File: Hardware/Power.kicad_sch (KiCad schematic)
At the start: 3 parts, among them J18 Conn_01x02

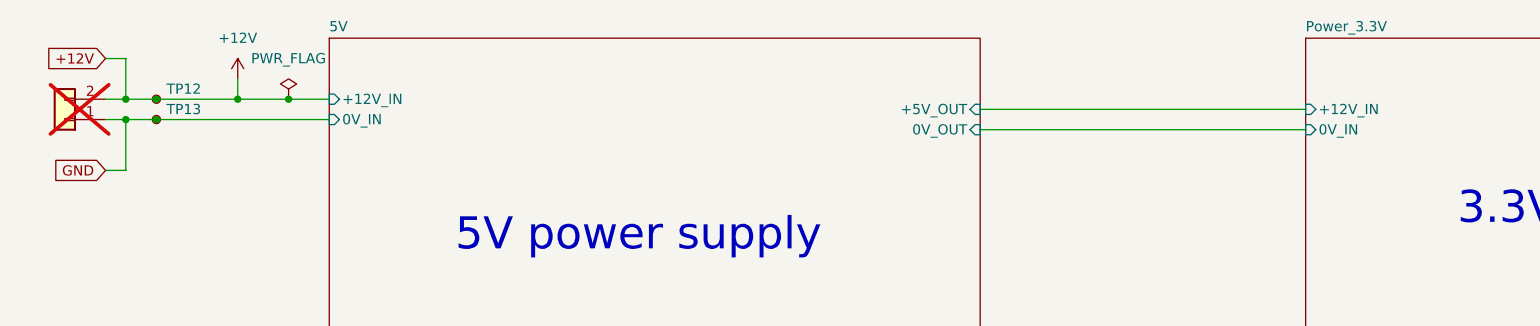
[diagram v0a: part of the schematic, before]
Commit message: Dodano diody TVS na każdej części zasilania, zmieniono bezpieczniki, podzielono bezpieczniki na bezpieczniki do prądów wewnętrznych oraz zewnętrznych,poprawiono małe błedy
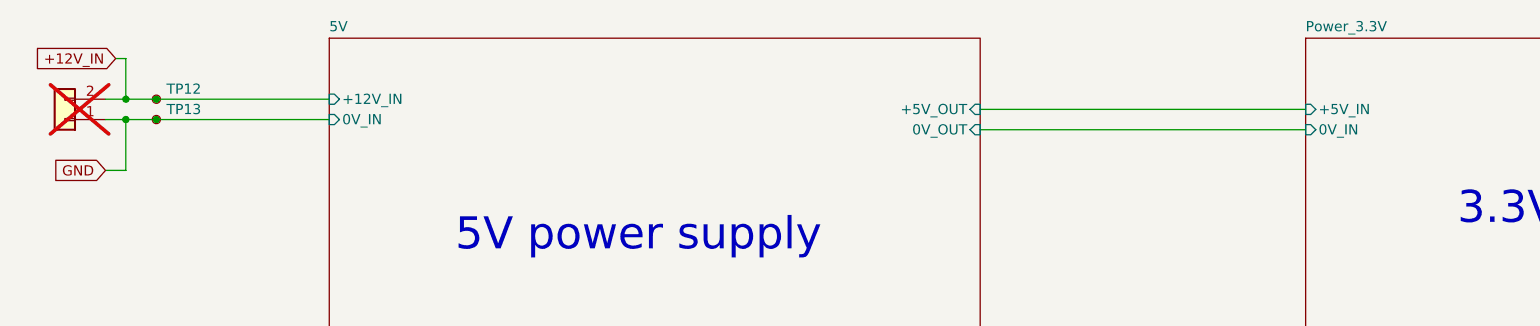
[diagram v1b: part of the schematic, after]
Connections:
- net +12V renamed +12V_IN
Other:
- sheet Power_3.3V ports: added +5V_IN; removed +12V_IN
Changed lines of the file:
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@@
 		(color 0 0 0 0)
 	)
-	(junction
-		(at 44.45 40.64)
-		(diameter 0)
-		(color 0 0 0 0)
-	)
-	(junction
-		(at 38.1 40.64)
-		(diameter 0)
-		(color 0 0 0 0)
-	)
 	(wire
 		(pts
@@
 	(wire
 		(pts
-			(xy 21.59 35.56) (xy 24.13 35.56)
+			(xy 22.86 35.56) (xy 24.13 35.56)
 		)
 		(stroke
@@
 	(wire
 		(pts
-			(xy 27.94 40.64) (xy 38.1 40.64)
-		)
-		(stroke
-			(width 0)
-			(type default)
-		)
-	)
-	(wire
-		(pts
 			(xy 21.59 40.64) (xy 24.13 40.64)
 		)
@@
 	(wire
 		(pts
-			(xy 38.1 38.1) (xy 38.1 40.64)
-		)
-		(stroke
-			(width 0)
-			(type default)
-		)
-	)
-	(wire
-		(pts
-			(xy 38.1 40.64) (xy 44.45 40.64)
-		)
-		(stroke
-			(width 0)
-			(type default)
-		)
-	)
-	(wire
-		(pts
-			(xy 44.45 40.64) (xy 49.53 40.64)
-		)
-		(stroke
-			(width 0)
-			(type default)
-		)
-	)
-	(global_label "+12V"
+			(xy 27.94 40.64) (xy 49.53 40.64)
+		)
+		(stroke
+			(width 0)
+			(type default)
+		)
+	)
+	(global_label "+12V_IN"
 		(shape input)
-		(at 21.59 35.56 180)
+		(at 22.86 35.56 180)
 		(fields_autoplaced yes)
 		(effects
@@
 		)
 		(property "Intersheetrefs" "${INTERSHEET_REFS}"
-			(at 13.5248 35.56 0)
+			(at 11.8919 35.56 0)
 			(effects
 				(font
@@
 				(justify right)
 				(hide yes)
-			)
-		)
-	)
-	(symbol
-		(lib_id "power:+12V")
-		(at 38.1 38.1 0)
-		(unit 1)
-		(exclude_from_sim no)
-		(in_bom yes)
-		(on_board yes)
-		(dnp no)
-		(fields_autoplaced yes)
-		(property "Reference" "#PWR0155"
-			(at 38.1 41.91 0)
-			(effects
-				(font
-					(size 1.27 1.27)
-				)
-				(hide yes)
-			)
-		)
-		(property "Value" "+12V"
-			(at 38.1 33.02 0)
-			(effects
-				(font
-					(size 1.27 1.27)
-				)
-			)
-		)
-		(property "Footprint" ""
-			(at 38.1 38.1 0)
-			(effects
-				(font
-					(size 1.27 1.27)
-				)
-				(hide yes)
-			)
-		)
-		(property "Datasheet" ""
-			(at 38.1 38.1 0)
-			(effects
-				(font
-					(size 1.27 1.27)
-				)
-				(hide yes)
-			)
-		)
-		(property "Description" "Power symbol creates a global label with name \"+12V\""
-			(at 38.1 38.1 0)
-			(effects
-				(font
-					(size 1.27 1.27)
-				)
-				(hide yes)
-			)
-		)
-		(pin "1"
-		)
-		(instances
-			(project "BMS"
-				(path "/26289bb6-56bc-4ca1-b1a2-18d58d1afdf5/b306fb08-ef5e-4bf5-8efa-c4e5200f566a"
-					(reference "#PWR0155")
-					(unit 1)
-				)
 			)
 		)
@@
 	)
 	(symbol
-		(lib_id "power:PWR_FLAG")
-		(at 44.45 40.64 0)
-		(unit 1)
-		(exclude_from_sim no)
-		(in_bom yes)
-		(on_board yes)
-		(dnp no)
-		(fields_autoplaced yes)
-		(property "Reference" "#FLG01"
-			(at 44.45 38.735 0)
-			(effects
-				(font
-					(size 1.27 1.27)
-				)
-				(hide yes)
-			)
-		)
-		(property "Value" "PWR_FLAG"
-			(at 44.45 35.56 0)
-			(effects
-				(font
-					(size 1.27 1.27)
-				)
-			)
-		)
-		(property "Footprint" ""
-			(at 44.45 40.64 0)
-			(effects
-				(font
-					(size 1.27 1.27)
-				)
-				(hide yes)
-			)
-		)
-		(property "Datasheet" "~"
-			(at 44.45 40.64 0)
-			(effects
-				(font
-					(size 1.27 1.27)
-				)
-				(hide yes)
-			)
-		)
-		(property "Description" "Special symbol for telling ERC where power comes from"
-			(at 44.45 40.64 0)
-			(effects
-				(font
-					(size 1.27 1.27)
-				)
-				(hide yes)
-			)
-		)
-		(pin "1"
-		)
-		(instances
-			(project "BMS"
-				(path "/26289bb6-56bc-4ca1-b1a2-18d58d1afdf5/b306fb08-ef5e-4bf5-8efa-c4e5200f566a"
-					(reference "#FLG01")
-					(unit 1)
-				)
-			)
-		)
-	)
-	(symbol
 		(lib_id "Connector_Generic:Conn_01x02")
 		(at 16.51 43.18 180)
@@
 			)
 		)
-		(pin "+12V_IN" input
+		(pin "+5V_IN" input
 			(at 171.45 41.91 180)
 			(effects

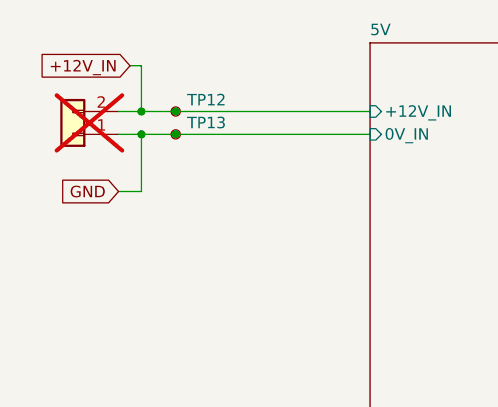
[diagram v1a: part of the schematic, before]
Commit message: dodano pozostale datasheety, zmieniono blad w usb
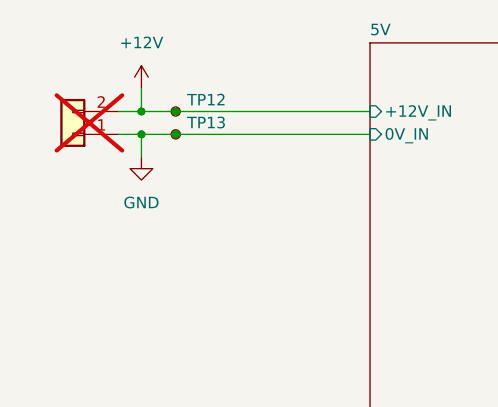
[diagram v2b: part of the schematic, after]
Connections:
- net +12V_IN renamed +12V
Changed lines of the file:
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@@
 	(wire
 		(pts
-			(xy 24.13 49.53) (xy 24.13 43.18)
-		)
-		(stroke
-			(width 0)
-			(type default)
-		)
-	)
-	(wire
-		(pts
-			(xy 22.86 35.56) (xy 24.13 35.56)
+			(xy 24.13 45.72) (xy 24.13 43.18)
 		)
 		(stroke
@@
 	(wire
 		(pts
-			(xy 21.59 49.53) (xy 24.13 49.53)
-		)
-		(stroke
-			(width 0)
-			(type default)
-		)
-	)
-	(wire
-		(pts
 			(xy 24.13 43.18) (xy 27.94 43.18)
 		)
@@
 	(wire
 		(pts
-			(xy 24.13 35.56) (xy 24.13 40.64)
+			(xy 24.13 38.1) (xy 24.13 40.64)
 		)
 		(stroke
@@
 			(width 0)
 			(type default)
-		)
-	)
-	(global_label "+12V_IN"
-		(shape input)
-		(at 22.86 35.56 180)
-		(fields_autoplaced yes)
-		(effects
-			(font
-				(size 1.27 1.27)
-			)
-			(justify right)
-		)
-		(property "Intersheetrefs" "${INTERSHEET_REFS}"
-			(at 11.8919 35.56 0)
-			(effects
-				(font
-					(size 1.27 1.27)
-				)
-				(justify right)
-				(hide yes)
-			)
-		)
-	)
-	(global_label "GND"
-		(shape input)
-		(at 21.59 49.53 180)
-		(fields_autoplaced yes)
-		(effects
-			(font
-				(size 1.27 1.27)
-			)
-			(justify right)
-		)
-		(property "Intersheetrefs" "${INTERSHEET_REFS}"
-			(at 14.7343 49.53 0)
-			(effects
-				(font
-					(size 1.27 1.27)
-				)
-				(justify right)
-				(hide yes)
-			)
 		)
 	)
@@
 	)
 	(symbol
+		(lib_id "power:+12V")
+		(at 24.13 38.1 0)
+		(unit 1)
+		(exclude_from_sim no)
+		(in_bom yes)
+		(on_board yes)
+		(dnp no)
+		(fields_autoplaced yes)
+		(property "Reference" "#PWR0136"
+			(at 24.13 41.91 0)
+			(effects
+				(font
+					(size 1.27 1.27)
+				)
+				(hide yes)
+			)
+		)
+		(property "Value" "+12V"
+			(at 24.13 33.02 0)
+			(effects
+				(font
+					(size 1.27 1.27)
+				)
+			)
+		)
+		(property "Footprint" ""
+			(at 24.13 38.1 0)
+			(effects
+				(font
+					(size 1.27 1.27)
+				)
+				(hide yes)
+			)
+		)
+		(property "Datasheet" ""
+			(at 24.13 38.1 0)
+			(effects
+				(font
+					(size 1.27 1.27)
+				)
+				(hide yes)
+			)
+		)
+		(property "Description" "Power symbol creates a global label with name \"+12V\""
+			(at 24.13 38.1 0)
+			(effects
+				(font
+					(size 1.27 1.27)
+				)
+				(hide yes)
+			)
+		)
+		(pin "1"
+		)
+		(instances
+			(project "BMS"
+				(path "/26289bb6-56bc-4ca1-b1a2-18d58d1afdf5/b306fb08-ef5e-4bf5-8efa-c4e5200f566a"
+					(reference "#PWR0136")
+					(unit 1)
+				)
+			)
+		)
+	)
+	(symbol
 		(lib_id "Connector:TestPoint_Small")
 		(at 27.94 43.18 0)
@@
 					(unit 1)
 				)
+			)
+		)
+	)
+	(symbol
+		(lib_id "power:GND")
+		(at 24.13 45.72 0)
+		(unit 1)
+		(exclude_from_sim no)
+		(in_bom yes)
+		(on_board yes)
+		(dnp no)
+		(fields_autoplaced yes)
+		(property "Reference" "#PWR0152"
+			(at 24.13 52.07 0)
+			(effects
+				(font
+					(size 1.27 1.27)
+				)
+				(hide yes)
+			)
+		)
+		(property "Value" "GND"
+			(at 24.13 50.8 0)
+			(effects
+				(font
+					(size 1.27 1.27)
+				)
+			)
+		)
+		(property "Footprint" ""
+			(at 24.13 45.72 0)
+			(effects
+				(font
+					(size 1.27 1.27)
+				)
+				(hide yes)
+			)
+		)
+		(property "Datasheet" ""
+			(at 24.13 45.72 0)
+			(effects
+				(font
+					(size 1.27 1.27)
+				)
+				(hide yes)
+			)
+		)
+		(property "Description" "Power symbol creates a global label with name \"GND\" , ground"
+			(at 24.13 45.72 0)
+			(effects
+				(font
+					(size 1.27 1.27)
+				)
+				(hide yes)
+			)
+		)
+		(pin "1"
+		)
+		(instances
+			(project "BMS"
+				(path "/26289bb6-56bc-4ca1-b1a2-18d58d1afdf5/b306fb08-ef5e-4bf5-8efa-c4e5200f566a"
+					(reference "#PWR0152")
+					(unit 1)
+				)

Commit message: Wiecej zmian wizualnych pod produkcje
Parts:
- removed TP12: TestPoint_Small, TestPoint:TestPoint_Pad_D1.0mm, symbol Connector:TestPoint_Small
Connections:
- net +12V renamed 12V_IN
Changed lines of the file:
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@@
-		(color 0 0 0 0)
-	)
-	(junction
-		(at 27.94 40.64)
-		(diameter 0)
 		(color 0 0 0 0)
 	)
@@
 	(wire
 		(pts
-			(xy 24.13 38.1) (xy 24.13 40.64)
+			(xy 24.13 35.56) (xy 24.13 40.64)
 		)
 		(stroke
@@
 		(pts
 			(xy 27.94 43.18) (xy 49.53 43.18)
-		)
-		(stroke
-			(width 0)
-			(type default)
-		)
-	)
-	(wire
-		(pts
-			(xy 24.13 40.64) (xy 27.94 40.64)
 		)
 		(stroke
@@
 	(wire
 		(pts
-			(xy 27.94 40.64) (xy 49.53 40.64)
+			(xy 22.86 35.56) (xy 24.13 35.56)
 		)
 		(stroke
@@
 		)
 	)
-	(symbol
-		(lib_id "Connector:TestPoint_Small")
-		(at 27.94 40.64 0)
-		(unit 1)
-		(exclude_from_sim no)
-		(in_bom yes)
-		(on_board yes)
-		(dnp no)
+	(wire
+		(pts
+			(xy 24.13 40.64) (xy 49.53 40.64)
+		)
+		(stroke
+			(width 0)
+			(type default)
+		)
+	)
+	(global_label "12V_IN"
+		(shape input)
+		(at 22.86 35.56 180)
 		(fields_autoplaced yes)
-		(property "Reference" "TP12"
-			(at 29.21 39.3699 0)
+		(effects
+			(font
+				(size 1.27 1.27)
+			)
+			(justify right)
+		)
+		(property "Intersheetrefs" "${INTERSHEET_REFS}"
+			(at 13.4643 35.56 0)
 			(effects
 				(font
 					(size 1.27 1.27)
 				)
-				(justify left)
+				(justify right)
+				(hide yes)
 			)
 		)
-		(property "Value" "TestPoint_Small"
-			(at 29.21 41.9099 0)
+		(property "Netclass" ""
+			(at 22.86 37.7508 0)
 			(effects
 				(font
 					(size 1.27 1.27)
 				)
-				(justify left)
+				(justify right)
 				(hide yes)
 			)
 		)
-		(property "Footprint" "TestPoint:TestPoint_Pad_D1.0mm"
-			(at 33.02 40.64 0)
-			(effects
-				(font
-					(size 1.27 1.27)
-				)
-				(hide yes)
-			)
-		)
-		(property "Datasheet" "~"
-			(at 33.02 40.64 0)
-			(effects
-				(font
-					(size 1.27 1.27)
-				)
-				(hide yes)
-			)
-		)
-		(property "Description" "test point"
-			(at 27.94 40.64 0)
-			(effects
-				(font
-					(size 1.27 1.27)
-				)
-				(hide yes)
-			)
-		)
-		(pin "1"
-		)
-		(instances
-			(project "BMS"
-				(path "/26289bb6-56bc-4ca1-b1a2-18d58d1afdf5/b306fb08-ef5e-4bf5-8efa-c4e5200f566a"
-					(reference "TP12")
-					(unit 1)
-				)
-			)
-		)
-	)
-	(symbol
-		(lib_id "power:+12V")
-		(at 24.13 38.1 0)
-		(unit 1)
-		(exclude_from_sim no)
-		(in_bom yes)
-		(on_board yes)
-		(dnp no)
-		(fields_autoplaced yes)
-		(property "Reference" "#PWR0136"
-			(at 24.13 41.91 0)
-			(effects
-				(font
-					(size 1.27 1.27)
-				)
-				(hide yes)
-			)
-		)
-		(property "Value" "+12V"
-			(at 24.13 33.02 0)
-			(effects
-				(font
-					(size 1.27 1.27)
-				)
-			)
-		)
-		(property "Footprint" ""
-			(at 24.13 38.1 0)
-			(effects
-				(font
-					(size 1.27 1.27)
-				)
-				(hide yes)
-			)
-		)
-		(property "Datasheet" ""
-			(at 24.13 38.1 0)
-			(effects
-				(font
-					(size 1.27 1.27)
-				)
-				(hide yes)
-			)
-		)
-		(property "Description" "Power symbol creates a global label with name \"+12V\""
-			(at 24.13 38.1 0)
-			(effects
-				(font
-					(size 1.27 1.27)
-				)
-				(hide yes)
-			)
-		)
-		(pin "1"
-		)
-		(instances
-			(project "BMS"
-				(path "/26289bb6-56bc-4ca1-b1a2-18d58d1afdf5/b306fb08-ef5e-4bf5-8efa-c4e5200f566a"
-					(reference "#PWR0136")
-					(unit 1)
-				)
-			)
-		)

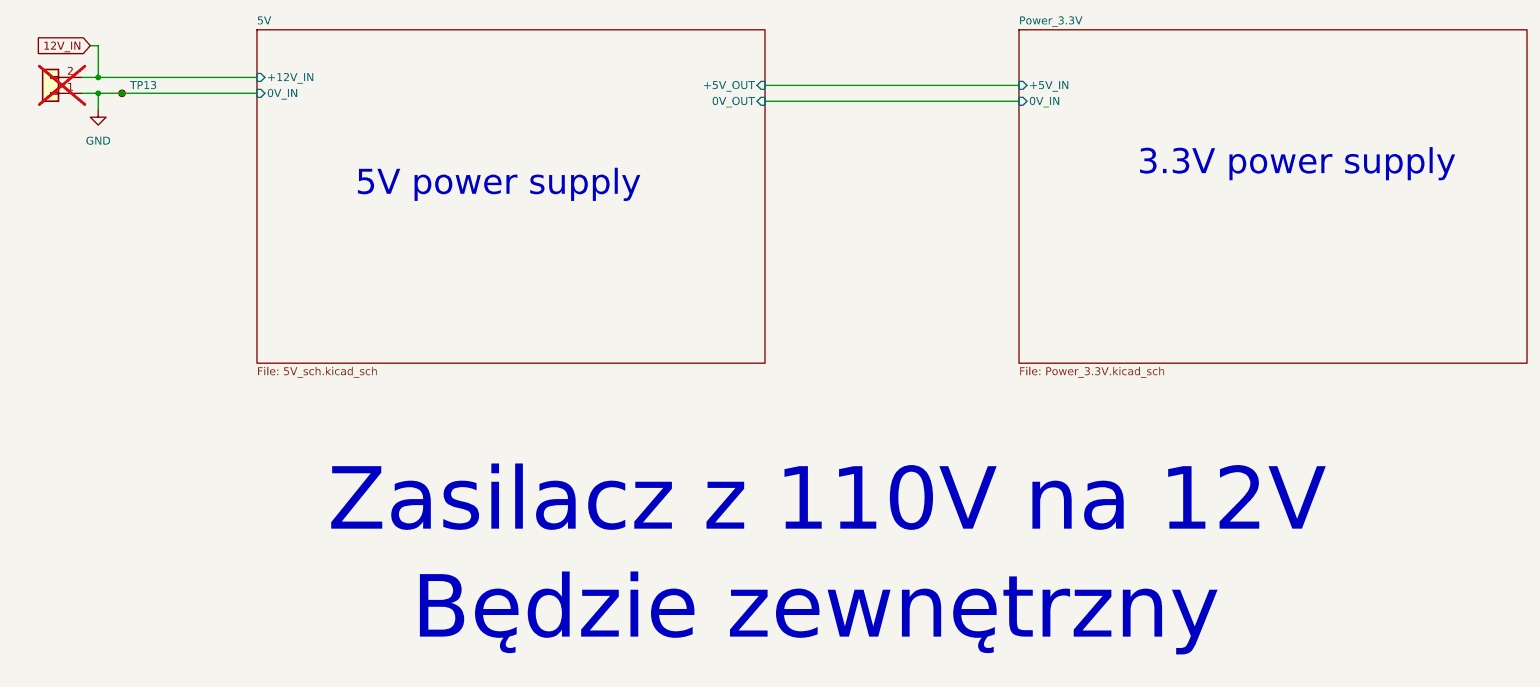
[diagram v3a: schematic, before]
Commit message: Zmiany wizualne w schemacie
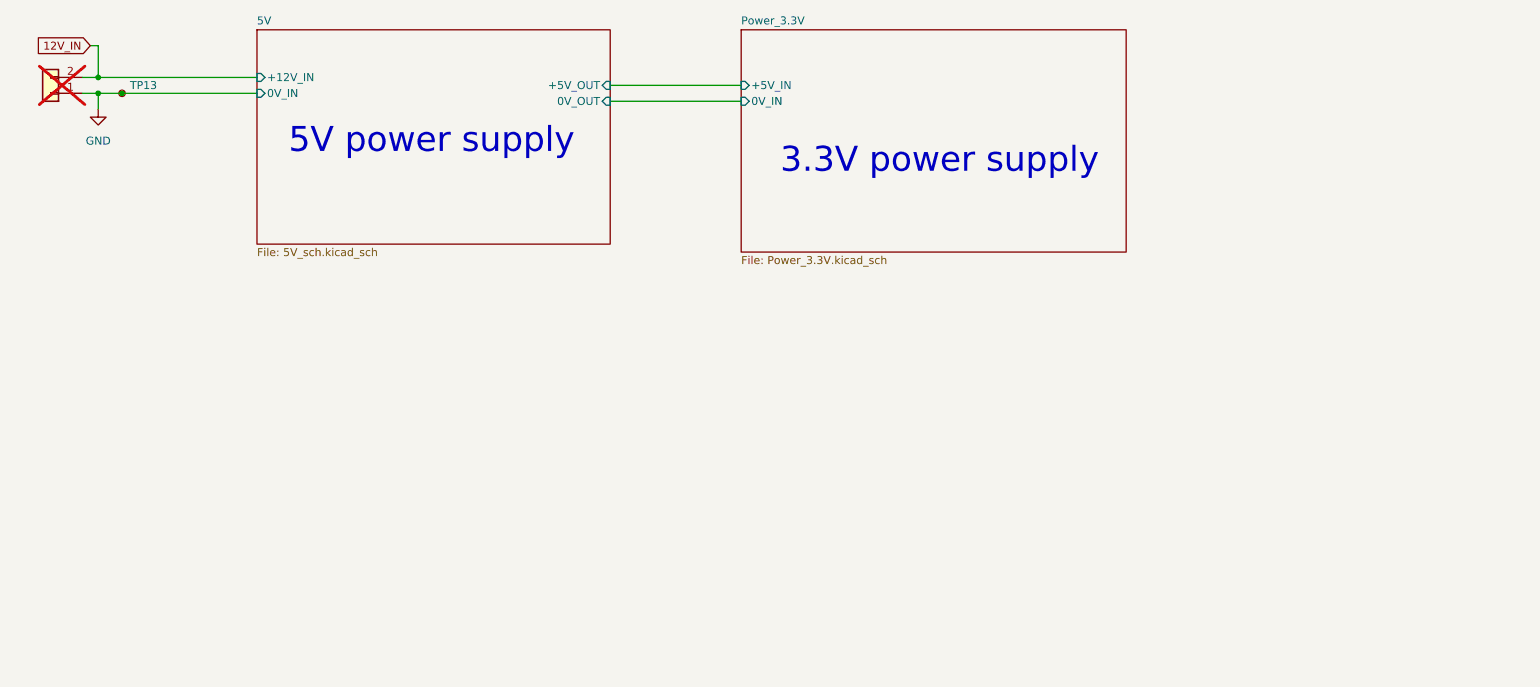
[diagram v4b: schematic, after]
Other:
- note removed: "Będzie zewnętrzny"
- note removed: "Zasilacz z 110V na 12V"
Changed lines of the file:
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@@
 	(generator "eeschema")
 	(generator_version "9.0")
-	(paper "A4")
-	(text "Zasilacz z 110V na 12V "
-		(exclude_from_sim no)
-		(at 140.716 108.458 0)
-		(effects
-			(font
-				(size 10 10)
-			)
-		)
-	)
-	(text "Będzie zewnętrzny"
-		(exclude_from_sim no)
-		(at 138.938 125.73 0)
-		(effects
-			(font
-				(size 10 10)
-			)
-		)
-	)
+	(paper "A5")
 	(text "5V power supply\n"
 		(exclude_from_sim no)
-		(at 88.138 57.658 0)
+		(at 77.47 50.8 0)
 		(effects
 			(font
@@
 	(text "3.3V power supply\n"
 		(exclude_from_sim no)
-		(at 215.9 54.356 0)
+		(at 158.75 53.975 0)
 		(effects
 			(font
@@
 	(wire
 		(pts
-			(xy 130.81 41.91) (xy 171.45 41.91)
+			(xy 106.045 41.91) (xy 127 41.91)
 		)
 		(stroke
@@
 	(wire
 		(pts
-			(xy 130.81 44.45) (xy 171.45 44.45)
+			(xy 106.045 44.45) (xy 127 44.45)
 		)
 		(stroke
@@
 	(sheet
 		(at 49.53 33.02)
-		(size 81.28 53.34)
+		(size 56.515 34.29)
 		(exclude_from_sim no)
 		(in_bom yes)
@@
 		)
 		(property "Sheetfile" "5V_sch.kicad_sch"
-			(at 49.53 86.9446 0)
+			(at 49.53 67.8946 0)
 			(effects
 				(font
@@
 		)
 		(pin "0V_OUT" input
-			(at 130.81 44.45 0)
+			(at 106.045 44.45 0)
 			(effects
 				(font
@@
 		)
 		(pin "+5V_OUT" input
-			(at 130.81 41.91 0)
+			(at 106.045 41.91 0)
 			(effects
 				(font
@@
 	)
 	(sheet
-		(at 171.45 33.02)
-		(size 81.28 53.34)
+		(at 127 33.02)
+		(size 61.595 35.56)
 		(exclude_from_sim no)
 		(in_bom yes)
@@
 		)
 		(property "Sheetname" "Power_3.3V"
-			(at 171.45 32.3084 0)
+			(at 127 32.3084 0)
 			(effects
 				(font
@@
 		)
 		(property "Sheetfile" "Power_3.3V.kicad_sch"
-			(at 171.45 86.9446 0)
+			(at 127 69.1646 0)
 			(effects
 				(font
@@
 		)
 		(pin "0V_IN" input
-			(at 171.45 44.45 180)
+			(at 127 44.45 180)
 			(effects
 				(font
@@
 		)
 		(pin "+5V_IN" input
-			(at 171.45 41.91 180)
-			(effects
-				(font
+			(at 127 41.91 180)
+			(effects
+				(font
